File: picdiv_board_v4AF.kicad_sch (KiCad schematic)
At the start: 56 parts, among them J1 DC-Input, J10 PPS_B, J101 MountingHole_M2.5, J104 MountingHole_M2.5, J105 Conn_01x06, J106 PPS_A, J107 PPS_A, J14 TEST_1PPS, J4 SYNC, J6 PPS_B, J8 SYNC, SW101 SW_DIP_x03, U1 LT1963AxST-3.3, U104 LTC6993xS6-1, U105 IDT5PB1108, U2 LT1963AxST-3.3, U6 IDT5PB1108, U8 PIC12F675-xMC

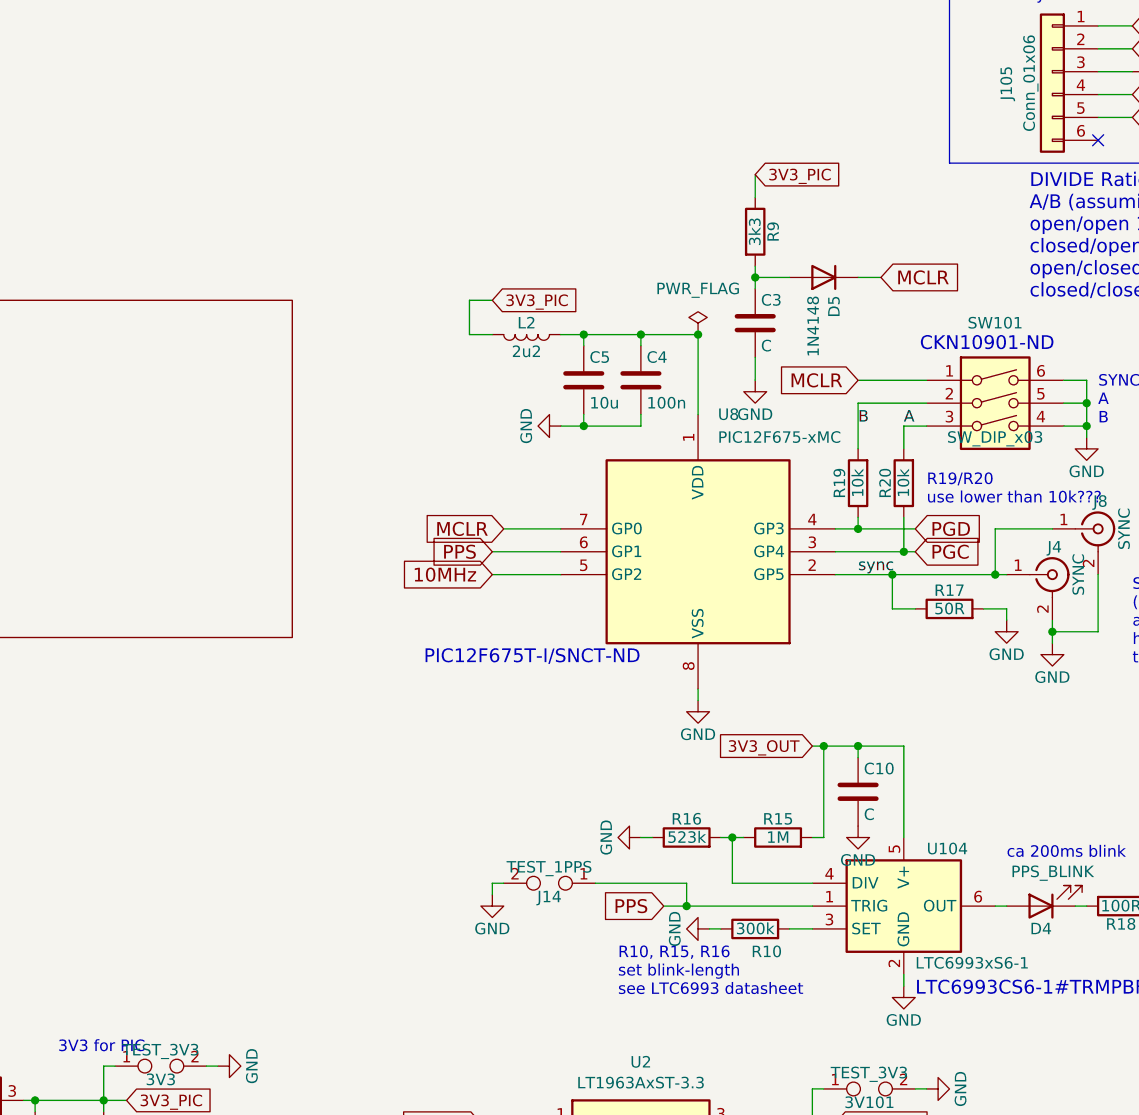
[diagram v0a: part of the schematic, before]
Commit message: Add missing footprints
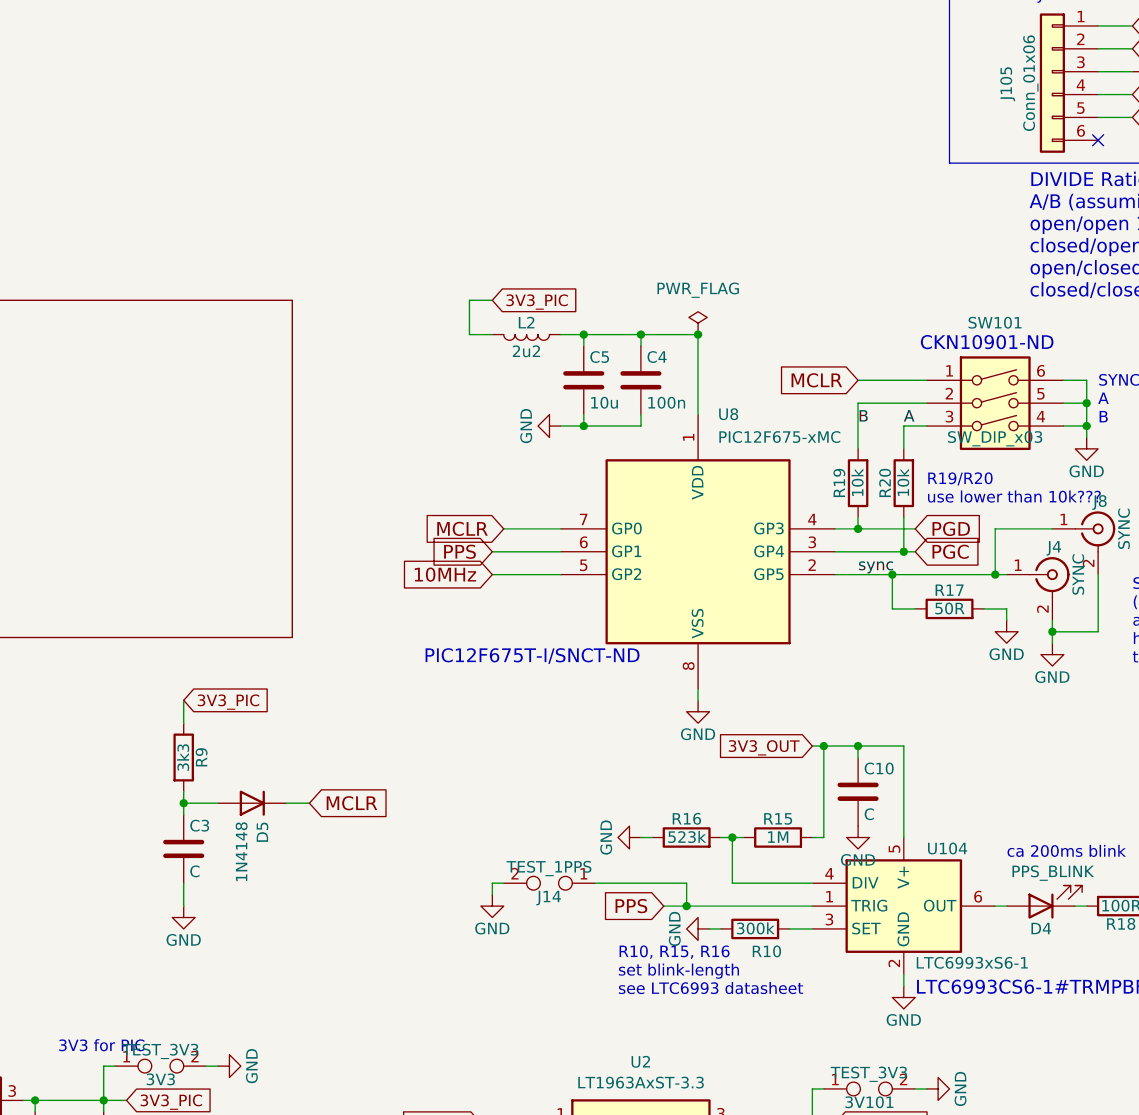
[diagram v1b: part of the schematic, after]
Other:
- moved on the sheet: C3, D5, R9
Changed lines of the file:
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@@
 	)
 	(junction
-		(at 134.62 46.99)
+		(at 71.12 105.41)
 		(diameter 0)
 		(color 0 0 0 0)
@@
 	(wire
 		(pts
-			(xy 148.59 46.99) (xy 146.05 46.99)
+			(xy 85.09 105.41) (xy 82.55 105.41)
 		)
 		(stroke
@@
 	(wire
 		(pts
-			(xy 134.62 45.72) (xy 134.62 46.99)
+			(xy 71.12 104.14) (xy 71.12 105.41)
 		)
 		(stroke
@@
 	(wire
 		(pts
-			(xy 138.43 46.99) (xy 134.62 46.99)
+			(xy 74.93 105.41) (xy 71.12 105.41)
 		)
 		(stroke
@@
 	(wire
 		(pts
-			(xy 134.62 58.42) (xy 134.62 55.88)
+			(xy 71.12 116.84) (xy 71.12 114.3)
 		)
 		(stroke
@@
 	(wire
 		(pts
-			(xy 134.62 46.99) (xy 134.62 48.26)
+			(xy 71.12 105.41) (xy 71.12 106.68)
 		)
 		(stroke
@@
 	(wire
 		(pts
-			(xy 134.62 38.1) (xy 134.62 35.56)
+			(xy 71.12 96.52) (xy 71.12 93.98)
 		)
 		(stroke
@@
 	(global_label "3V3_PIC"
 		(shape input)
-		(at 134.62 35.56 0)
+		(at 71.12 93.98 0)
 		(fields_autoplaced yes)
 		(effects
@@
 		)
 		(property "Intersheetrefs" "${INTERSHEET_REFS}"
-			(at 144.4916 35.56 0)
+			(at 80.9916 93.98 0)
 			(effects
 				(font
@@
 	(global_label "MCLR"
 		(shape input)
-		(at 148.59 46.99 0)
+		(at 85.09 105.41 0)
 		(fields_autoplaced yes)
 		(effects
@@
 		)
 		(property "Intersheetrefs" "${INTERSHEET_REFS}"
-			(at 157.3148 46.99 0)
+			(at 93.8148 105.41 0)
 			(effects
 				(font
@@
 	(symbol
 		(lib_id "Device:R")
-		(at 134.62 41.91 0)
+		(at 71.12 100.33 0)
 		(unit 1)
 		(exclude_from_sim no)
@@
 		(dnp no)
 		(property "Reference" "R9"
-			(at 136.652 41.91 90)
+			(at 73.152 100.33 90)
 			(effects
 				(font
@@
 		)
 		(property "Value" "3k3"
-			(at 134.62 41.91 90)
+			(at 71.12 100.33 90)
 			(effects
 				(font
@@
 		)
 		(property "Footprint" "Resistor_SMD:R_0805_2012Metric"
-			(at 132.842 41.91 90)
+			(at 69.342 100.33 90)
 			(effects
 				(font
@@
 		)
 		(property "Datasheet" "~"
-			(at 134.62 41.91 0)
+			(at 71.12 100.33 0)
 			(effects
 				(font
@@
 		)
 		(property "Description" "Resistor"
-			(at 134.62 41.91 0)
+			(at 71.12 100.33 0)
 			(effects
 				(font
@@
 	(symbol
 		(lib_id "Device:C")
-		(at 134.62 52.07 0)
+		(at 71.12 110.49 0)
 		(unit 1)
 		(exclude_from_sim no)
@@
 		(dnp no)
 		(property "Reference" "C3"
-			(at 135.255 49.53 0)
+			(at 71.755 107.95 0)
 			(effects
 				(font
@@
 		)
 		(property "Value" "C"
-			(at 135.255 54.61 0)
+			(at 71.755 113.03 0)
 			(effects
 				(font
@@
 		)
 		(property "Footprint" "Capacitor_SMD:C_0805_2012Metric"
-			(at 135.5852 55.88 0)
+			(at 72.0852 114.3 0)
 			(effects
 				(font
@@
 		)
 		(property "Datasheet" "~"
-			(at 134.62 52.07 0)
+			(at 71.12 110.49 0)
 			(effects
 				(font
@@
 		)
 		(property "Description" "Unpolarized capacitor"
-			(at 134.62 52.07 0)
+			(at 71.12 110.49 0)
 			(effects
 				(font
@@
 	(symbol
 		(lib_id "power:GND")
-		(at 134.62 58.42 0)
+		(at 71.12 116.84 0)
 		(unit 1)
 		(exclude_from_sim no)
@@
 		(dnp no)
 		(property "Reference" "#PWR019"
-			(at 134.62 64.77 0)
+			(at 71.12 123.19 0)
 			(effects
 				(font
@@
 		)
 		(property "Value" "GND"
-			(at 134.62 62.23 0)
+			(at 71.12 120.65 0)
 			(effects
 				(font
@@
 		)
 		(property "Footprint" ""
-			(at 134.62 58.42 0)
+			(at 71.12 116.84 0)
 			(effects
 				(font
@@
 		)
 		(property "Datasheet" ""
-			(at 134.62 58.42 0)
+			(at 71.12 116.84 0)
 			(effects
 				(font
@@
 		)
 		(property "Description" "Power symbol creates a global label with name \"GND\" , ground"
-			(at 134.62 58.42 0)
+			(at 71.12 116.84 0)
 			(effects
 				(font
@@
 	(symbol
 		(lib_id "Device:D")
-		(at 142.24 46.99 180)
+		(at 78.74 105.41 180)
 		(unit 1)
 		(exclude_from_sim yes)
@@
 		(dnp no)
 		(property "Reference" "D5"
-			(at 143.4084 48.9966 90)
+			(at 79.9084 107.4166 90)
 			(effects
 				(font
@@
 		)
 		(property "Value" "1N4148"
-			(at 141.097 48.9966 90)
+			(at 77.597 107.4166 90)
 			(effects
 				(font
@@
 		)
 		(property "Footprint" "Diodes_SMD:D_SOD-123"
-			(at 142.24 46.99 0)
+			(at 78.74 105.41 0)
 			(effects
 				(font
@@
 		)
 		(property "Datasheet" "~"
-			(at 142.24 46.99 0)
+			(at 78.74 105.41 0)
 			(effects
 				(font
@@
 		)
 		(property "Description" "Diode"
-			(at 142.24 46.99 0)
+			(at 78.74 105.41 0)
 			(effects
 				(font
@@
 		)
 		(property "Sim.Device" "D"
-			(at 142.24 46.99 0)
+			(at 78.74 105.41 0)
 			(effects
 				(font
@@
 		)
 		(property "Sim.Pins" "1=K 2=A"
-			(at 142.24 46.99 0)
+			(at 78.74 105.41 0)
 			(effects
 				(font

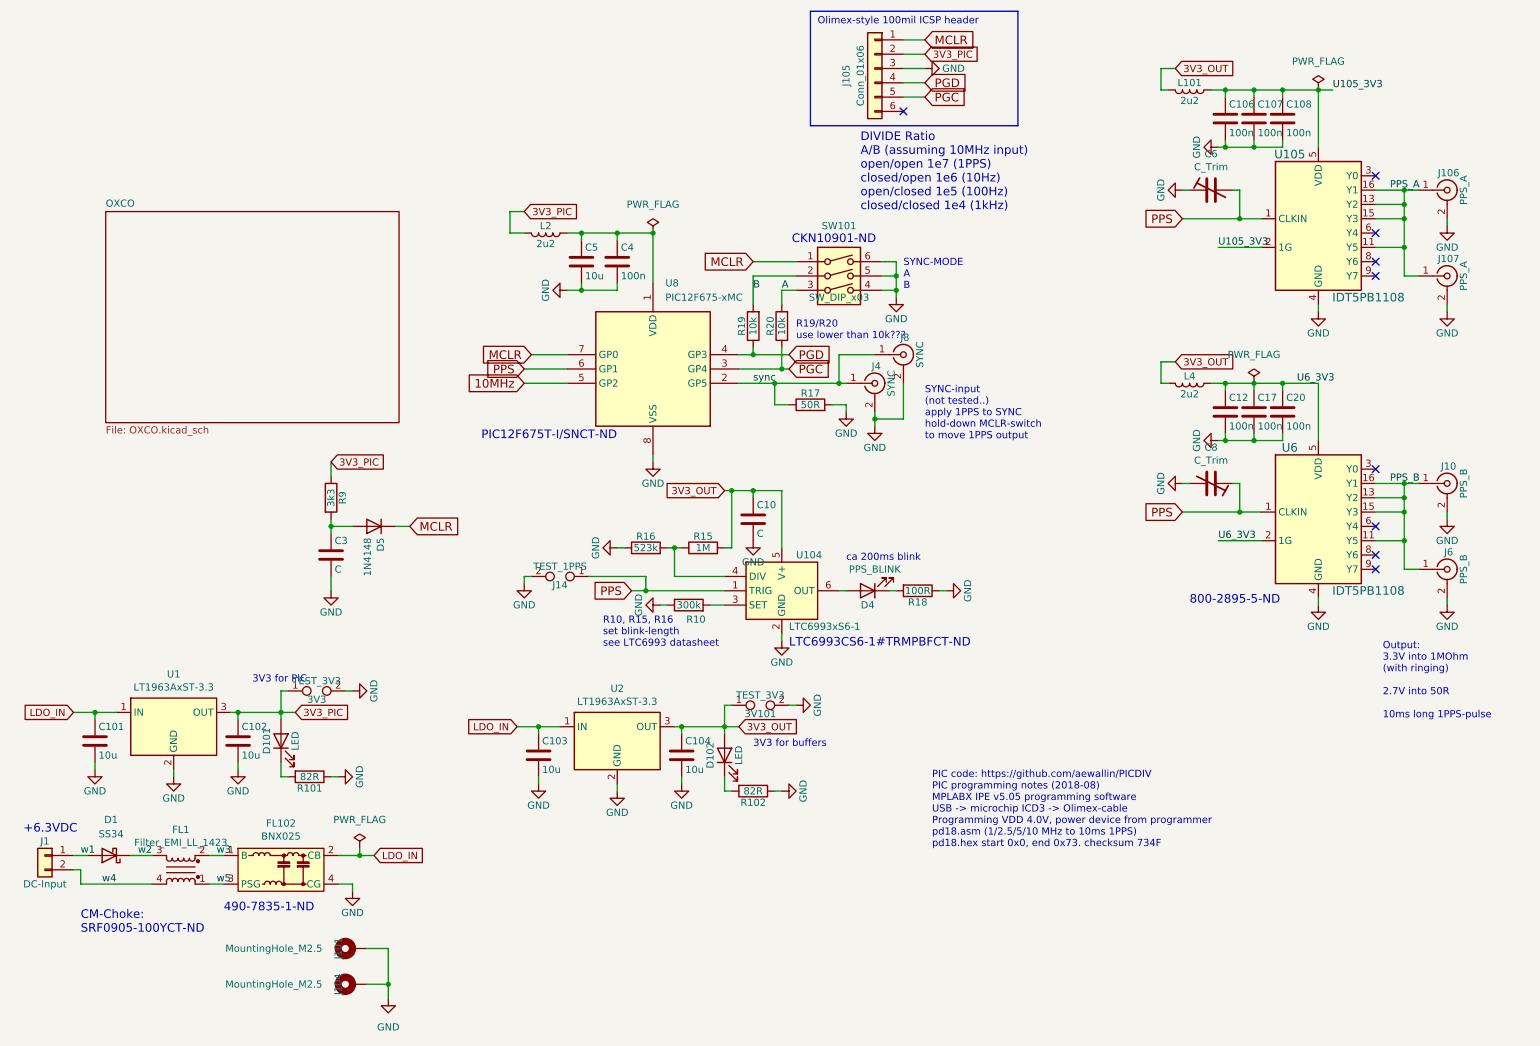
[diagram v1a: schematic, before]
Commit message: A bit of layout work
Remove sine to square parts from layout.  We don't need it.
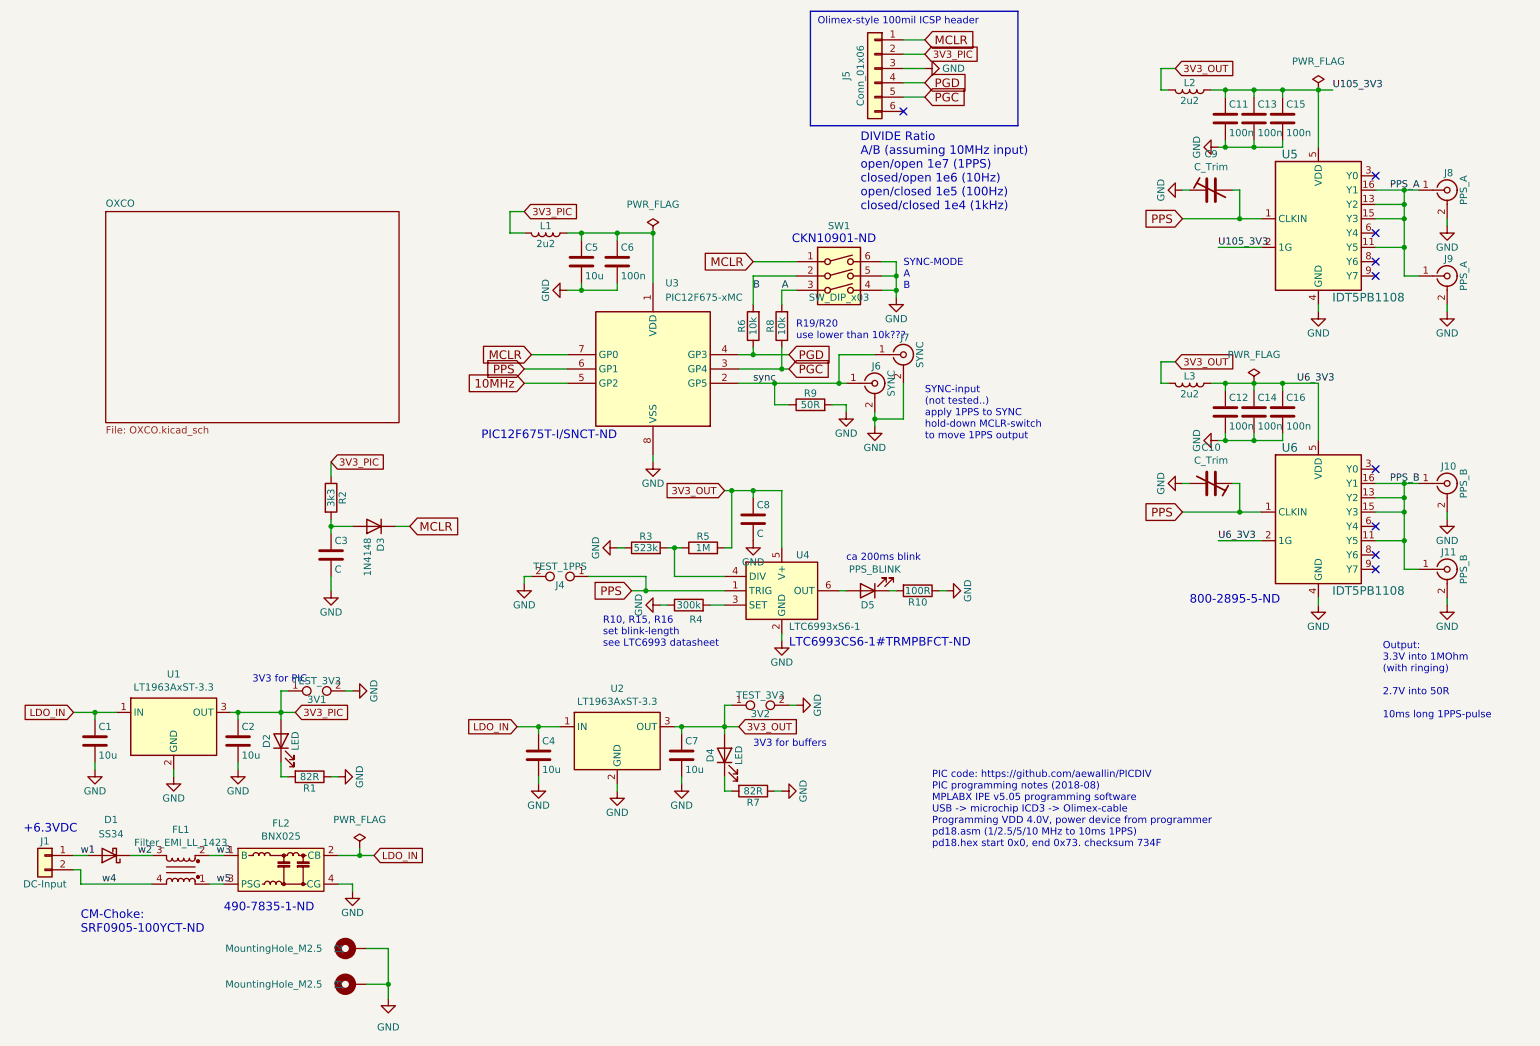
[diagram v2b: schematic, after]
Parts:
- renumbered 3V3 to 3V1, 3V101 to 3V2, C101 to C1, C8 to C10, C106 to C11, C107 to C13, C17 to C14, C108 to C15, C20 to C16, C102 to C2, C103 to C4, C4 to C6, C104 to C7, C10 to C8, C6 to C9, D101 to D2, D5 to D3, D102 to D4, D4 to D5, FL102 to FL2, J6 to J11, J101 to J2, J104 to J3, J14 to J4, J105 to J5, J4 to J6, J8 to J7, J106 to J8, J107 to J9, L2 to L1, L101 to L2, L4 to L3, R101 to R1, R18 to R10, R9 to R2, R16 to R3, R10 to R4, R15 to R5, R19 to R6, R102 to R7, R20 to R8, R17 to R9, SW101 to SW1, U8 to U3, U104 to U4, U105 to U5

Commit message: More Layout
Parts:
- removed J6: SYNC, Connector_Coaxial:SMA_Molex_73251-2200_Horizontal, symbol Connector:Conn_Coaxial
- removed J7: SYNC, Connector_Coaxial:BNC_Amphenol_B6252HB-NPP3G-50_Horizontal, symbol Connector:Conn_Coaxial
- removed U3: PIC12F675-xMC, Package_DFN_QFN:DFN-8-1EP_3x2mm_P0.5mm_EP1.7x1.4mm, symbol MCU_Microchip_PIC12:PIC12F675-xMC
- added U3: PIC12F675-xSN, Package_SO:SOIC-8_3.9x4.9mm_P1.27mm, symbol MCU_Microchip_PIC12:PIC12F675-xSN
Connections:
- net 10MHz: now also U3.5 (GP2)
- net GND: now also U3.8 (VSS)
- net MCLR: now also U3.7 (GP0)
- net PGC: now also U3.3 (GP4)
- net PGD: now also U3.4 (GP3)
- net PPS: now also U3.6 (GP1)
- net sync: now also U3.2 (GP5)
- net at C5.1, C6.1, L1.1: now also U3.1 (VDD)
